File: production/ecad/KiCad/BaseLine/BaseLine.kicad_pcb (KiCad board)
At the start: 4 copper layers, 105.8 x 119.5 mm, 120 parts, among them IC1 AP7362-33SP-13 (3.3V LDO), J1 VibeMotorConnector_1, J10 LoadCell1, J11 LoadCell2, J12 LoadCell3, J13 LoadCell4, J14 Power_to_Loadcell, J17 IMU_connector, J2 1332645, J3 Conn_01x02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

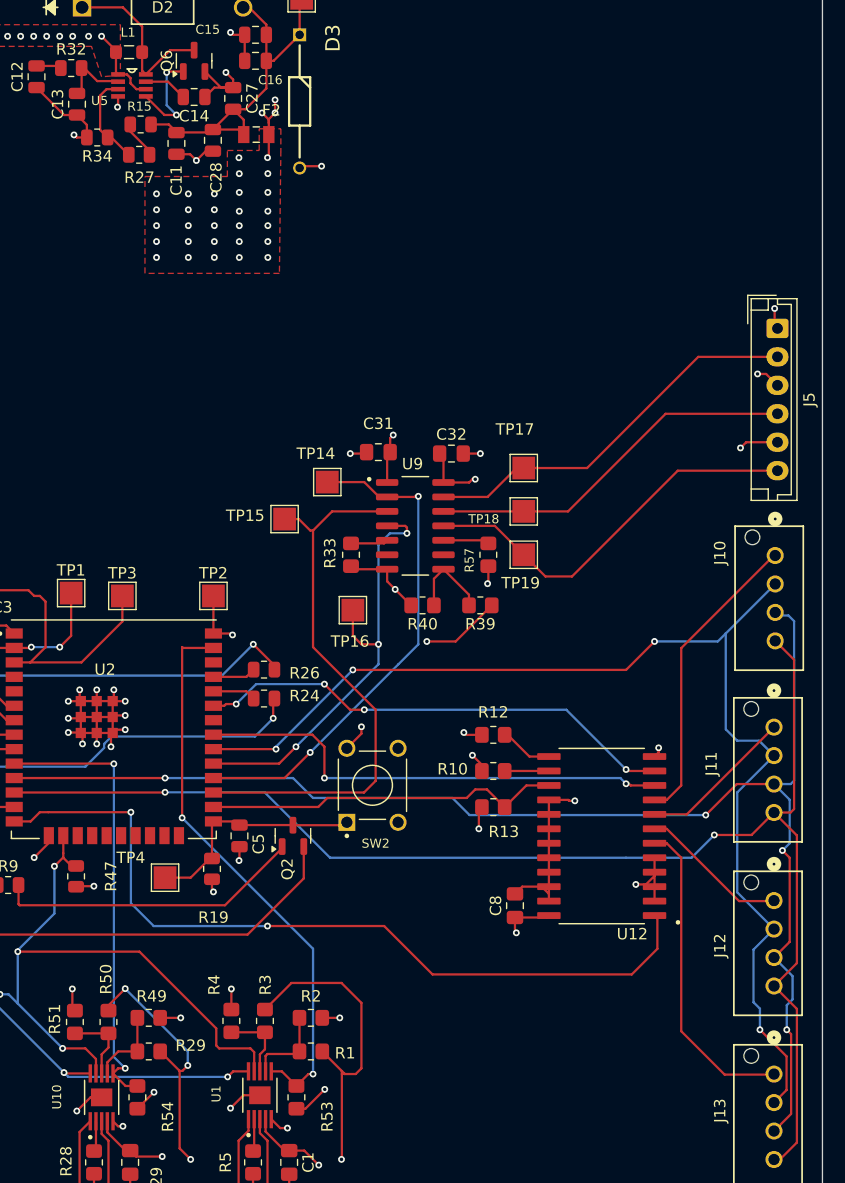
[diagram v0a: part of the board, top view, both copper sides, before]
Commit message: minor routing fixes
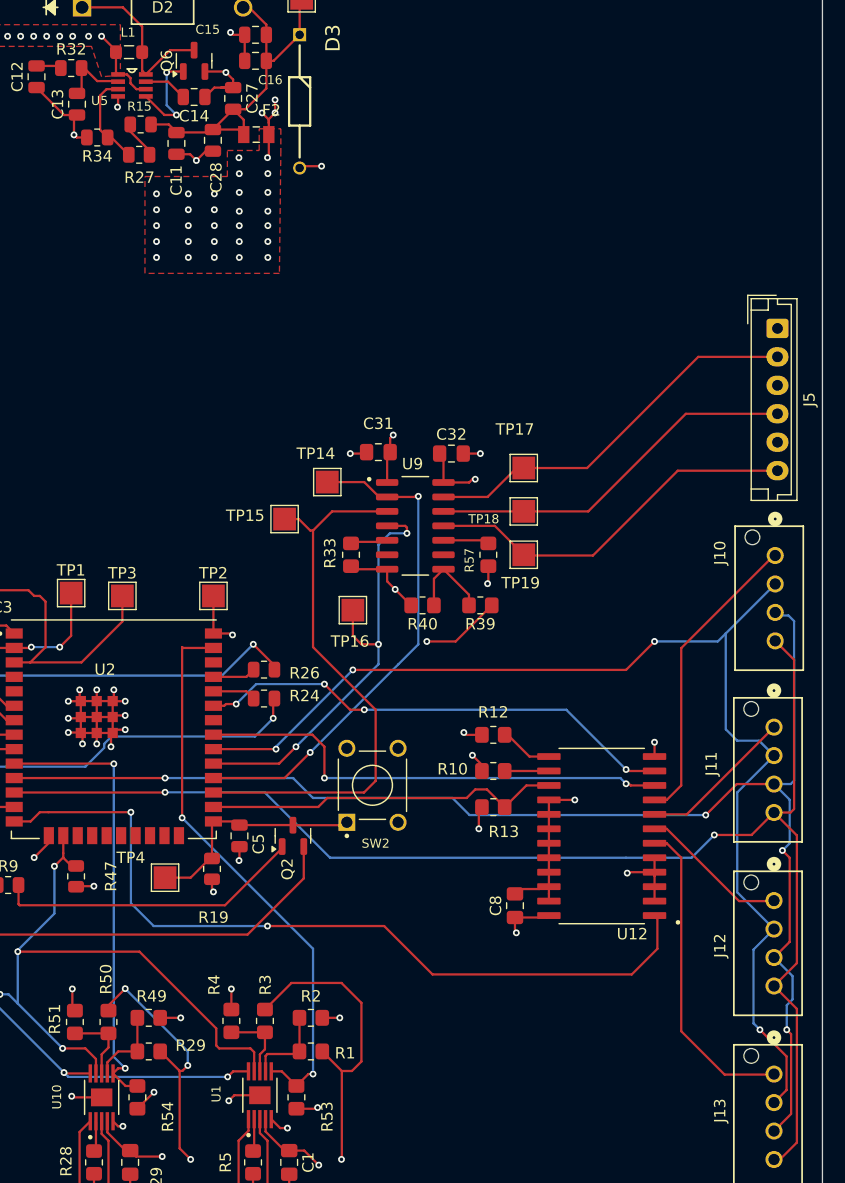
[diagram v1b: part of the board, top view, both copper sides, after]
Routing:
- net GND: track 216.6 -> 209.9 mm, vias 66 -> 63
- net +5V: track 87.9 -> 83.8 mm, vias 42 -> 41
- net Net-(J5-Pin_6): track 35.0 -> 33.5 mm
- net +3.3V: track 66.8 -> 65.5 mm

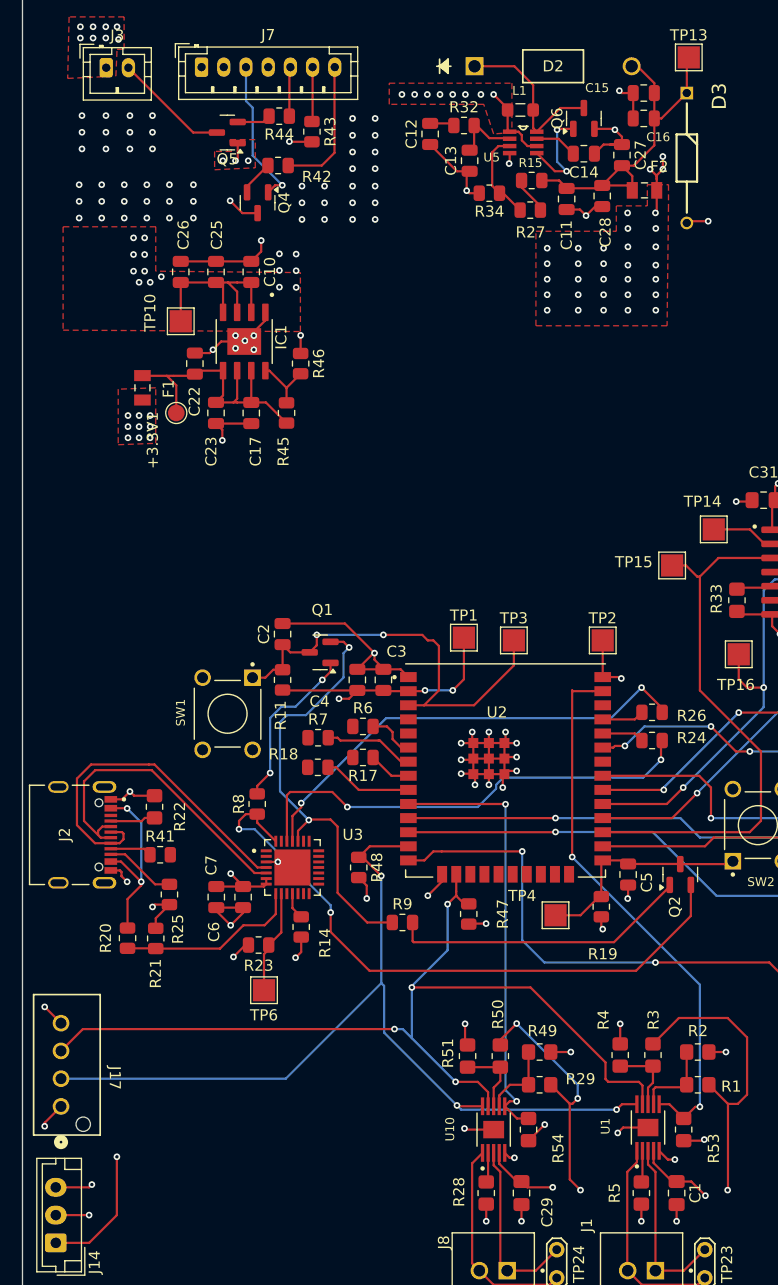
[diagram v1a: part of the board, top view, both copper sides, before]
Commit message: DRC fixes - clearances
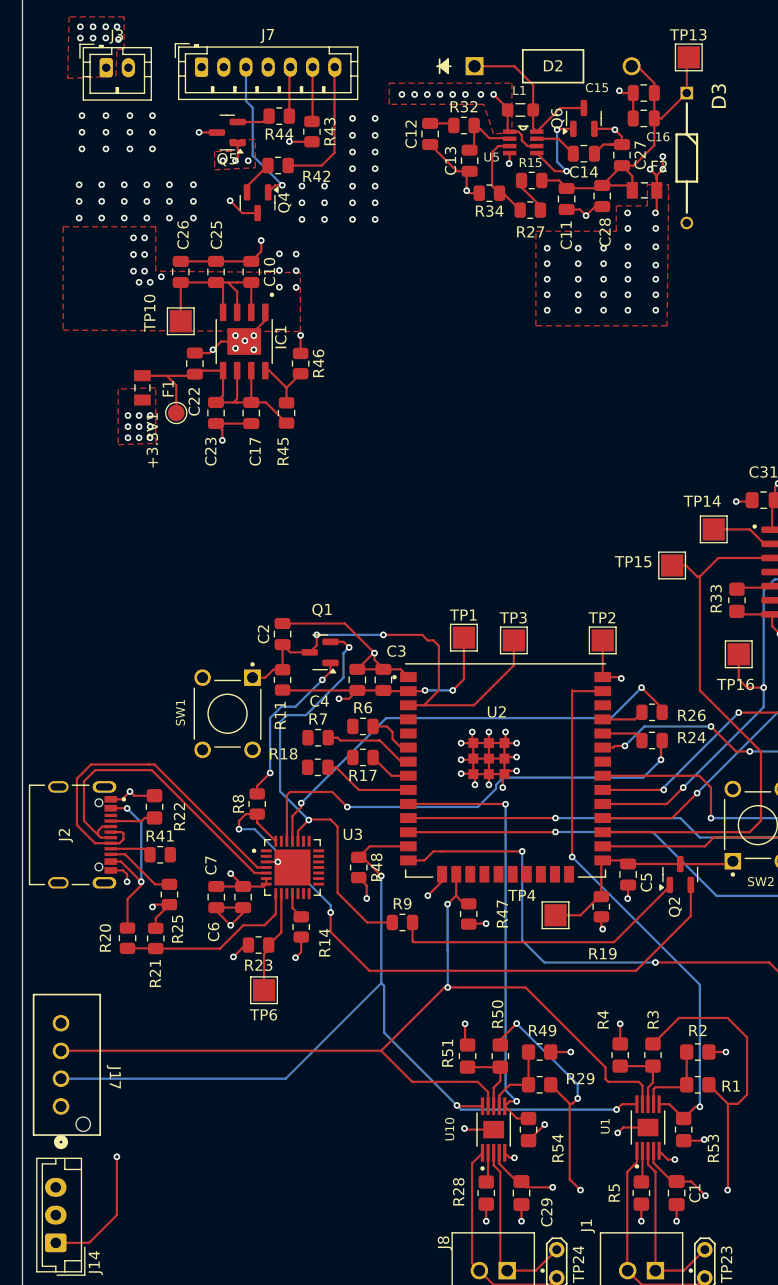
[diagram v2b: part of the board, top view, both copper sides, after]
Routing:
- net GND: track 209.9 -> 194.1 mm, vias 63 -> 61
- net +5V: track 83.8 -> 80.8 mm, vias 41 -> 40
- net SDA: track 87.7 -> 85.1 mm, vias 4 -> 2
- net +3.3V: track 65.5 -> 63.1 mm, vias 23 -> 22

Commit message: routing improvements
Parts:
- moved TP3 0.25 mm to (100.2, 102.0)
- moved TP2 0.15 mm to (108.2, 102.1)
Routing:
- net GND: track 194.1 -> 159.1 mm, vias 61 -> 69
- net +3.7V: track 27.5 -> 9.20 mm
- net USB_D+: track 32.3 -> 18.0 mm, vias 0 -> 2
- net USB_D-: track 29.0 -> 18.2 mm
- net Net-(Q6-G): track 9.34 -> 5.72 mm
- net +5V: track 80.8 -> 79.1 mm
- net Net-(D2A-A): track 15.4 -> 14.4 mm
- net Net-(U3-RXD): track 41.7 -> 40.8 mm
- net Net-(D2A-K): track 33.8 -> 32.8 mm
- net Net-(J7-Pin_3): track 13.5 -> 12.8 mm
- net FAULTn_2: track 39.8 -> 39.2 mm
- added copper zone on F.Cu, net GND

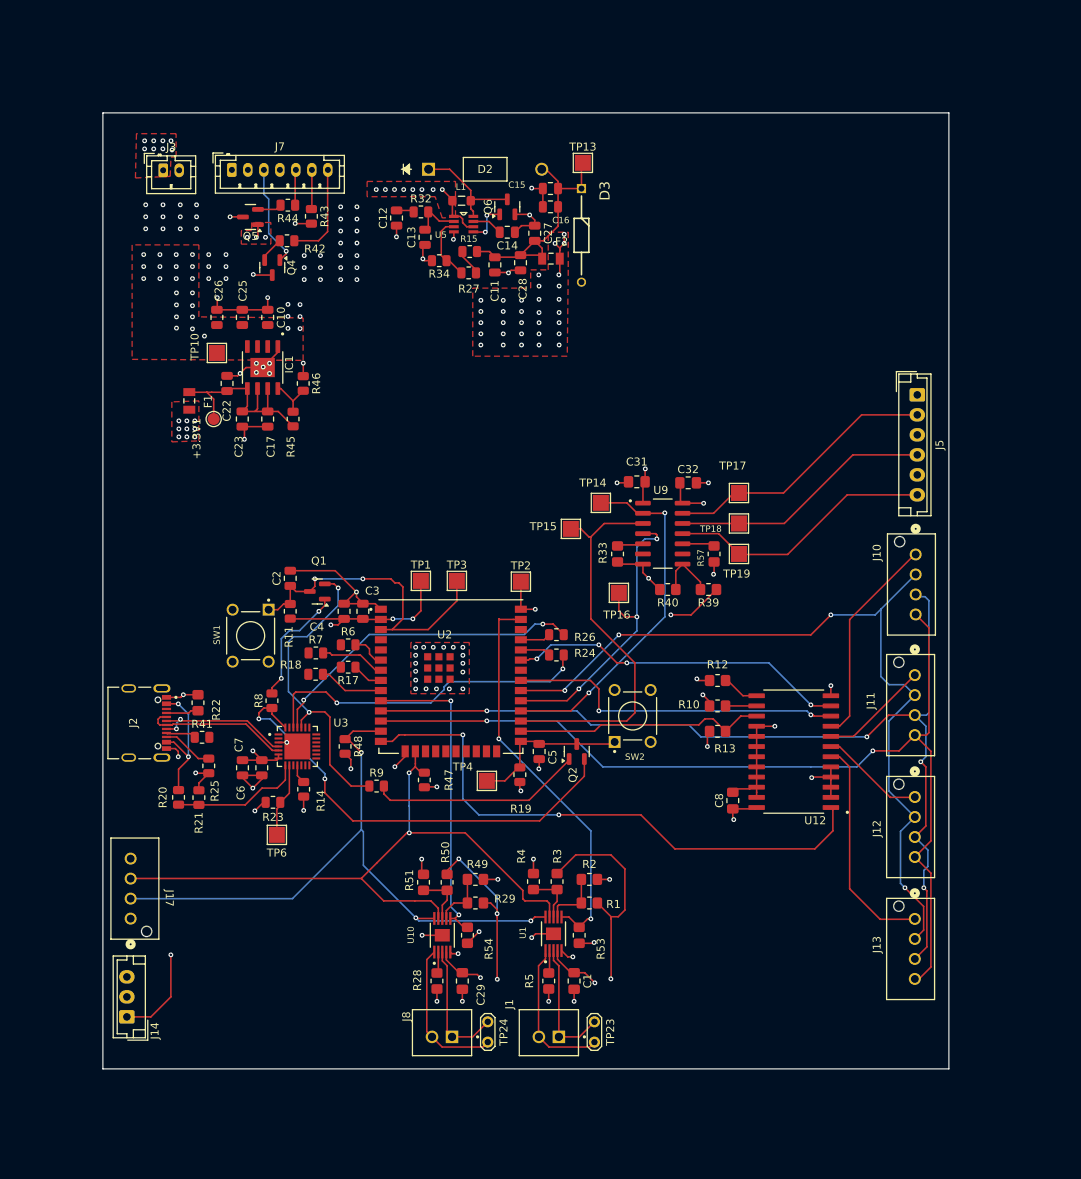
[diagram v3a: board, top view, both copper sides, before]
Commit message: differential pairing and minor changes
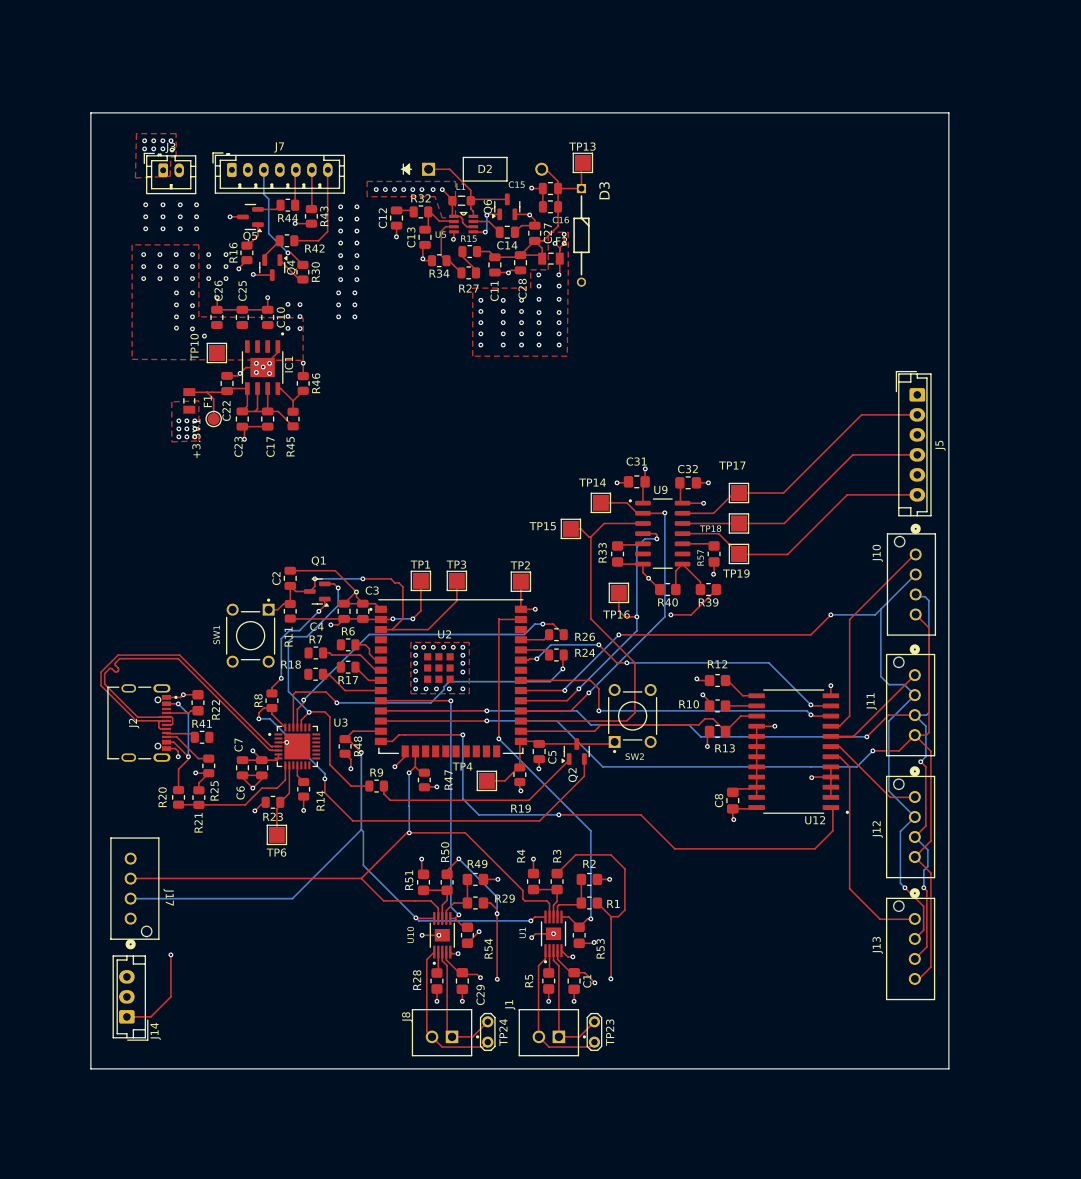
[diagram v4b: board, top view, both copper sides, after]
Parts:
- added R16: 0, Resistor_SMD:R_0805_2012Metric, F.Cu at (74.0, 61.0)
- added R30: 0, Resistor_SMD:R_0805_2012Metric, F.Cu at (81.0, 63.4)
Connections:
- Q4 pad 1: Net-(J7-Pin_3) -> Net-(Q4-G)
- Q5 pad 1: +3.7V -> Net-(Q5-G)
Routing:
- net USB_D+: track 18.0 -> 42.2 mm, vias 2 -> 0
- net USB_D-: track 18.2 -> 41.8 mm
- net Net-(Q4-G): track 0.00 -> 3.88 mm
- net Net-(Q5-G): track 0.00 -> 3.62 mm
- net Net-(J7-Pin_3): track 12.8 -> 14.1 mm
- net +3.7V: track 9.20 -> 8.70 mm, vias 84 -> 82
- net GND: vias 69 -> 71
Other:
- board size 105.8 x 119.5 mm -> 107.2 x 119.5 mm
